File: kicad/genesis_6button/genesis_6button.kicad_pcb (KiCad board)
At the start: 2 copper layers, 61.7 x 36.8 mm, 27 parts, among them J1 Conn_02x07_Odd_Even, J2 DB9_Female, J3 Conn_02x03_Odd_Even, U1 74HC257, U2 ATtiny404-SS, U3 74HC257

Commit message: Revert to first revision of PCB
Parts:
- removed C4: 10u, Capacitor_THT:CP_Radial_D8.0mm_P5.00mm
- removed H1: MountingHole, MountingHole:MountingHole_5.3mm_M5
- removed R13, R14: 100k, Resistor_SMD:R_0805_2012Metric
- removed TP1, TP2: TestPoint, TestPoint:TestPoint_Loop_D3.50mm_Drill0.9mm_Beaded
- C1, C2, C3: footprint Capacitor_SMD:C_1206_3216Metric -> Capacitor_SMD:C_0805_2012Metric
- R1, R10, R11, R12, R2, R3, R4, R5, R6, R7, R8, R9: value 75k -> 47k
- moved R4 16.5 mm to (108.0, 52.8), turned to 180 degrees
- moved R5 15.8 mm to (108.0, 50.3), turned to 180 degrees
- moved R11 14.4 mm to (108.0, 60.5), turned to 180 degrees
- moved R6 12.2 mm to (108.0, 47.8), turned to 180 degrees
- moved R12 11.4 mm to (108.0, 57.9), turned to 180 degrees
- moved R10 9.76 mm to (112.4, 60.5), turned to 0 degrees
- moved R7 9.15 mm to (108.0, 63.0), turned to 180 degrees
- moved R1 8.10 mm to (112.4, 52.8), turned to 0 degrees
- moved J1 8.05 mm to (97.2, 47.8)
- moved R3 7.22 mm to (112.4, 47.8), turned to 0 degrees
- moved R8 6.67 mm to (112.4, 63.0), turned to 0 degrees
- moved R9 6.43 mm to (112.4, 57.9), turned to 0 degrees
- moved J2 4.96 mm to (154.9, 45.8)
- moved R2 4.65 mm to (112.4, 50.3), turned to 0 degrees
- moved C1 4.31 mm to (131.7, 44.8), turned to 270 degrees
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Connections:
- U2 pad 3: BUTTON_MODE -> (no net)
- U3 pad 2: BUTTON_DOWN -> BUTTON_UP
- U3 pad 3: BUTTON_Y -> BUTTON_Z
- U3 pad 4: DOWN -> UP
- U3 pad 5: BUTTON_UP -> BUTTON_DOWN
- U3 pad 6: BUTTON_Z -> BUTTON_Y
- U3 pad 7: UP -> DOWN
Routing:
- net Net-(J3-Pad1): track 30.3 -> 77.9 mm, vias 1 -> 2
- net BUTTON_Z: track 35.9 -> 74.1 mm
- net BUTTON_Y: track 29.6 -> 64.9 mm, vias 1 -> 2
- net BUTTON_X: track 39.0 -> 71.4 mm, vias 3 -> 2
- net DOWN: track 52.2 -> 81.8 mm, vias 4 -> 1
- net +5V: track 138.6 -> 168.2 mm, vias 6 -> 5
- net BUTTON_LEFT: track 48.5 -> 69.0 mm, vias 2 -> 3
- net Net-(U2-Pad5): track 41.7 -> 28.9 mm
- net UP: track 66.3 -> 76.4 mm, vias 2 -> 1
- net BUTTON_C: track 21.0 -> 30.4 mm, vias 0 -> 1
- net BUTTON_DOWN: track 25.0 -> 34.1 mm
- net BUTTON_B: track 22.6 -> 31.2 mm, vias 0 -> 1
- net BUTTON_A: track 25.9 -> 34.0 mm, vias 2 -> 3
- net BUTTON_UP: track 22.7 -> 29.0 mm
- net RIGHT: track 52.7 -> 46.6 mm, vias 3 -> 2
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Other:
- board size 61.7 x 36.8 mm -> 73.7 x 36.8 mm
- board text removed: "+5V"
- board text removed: "GND"

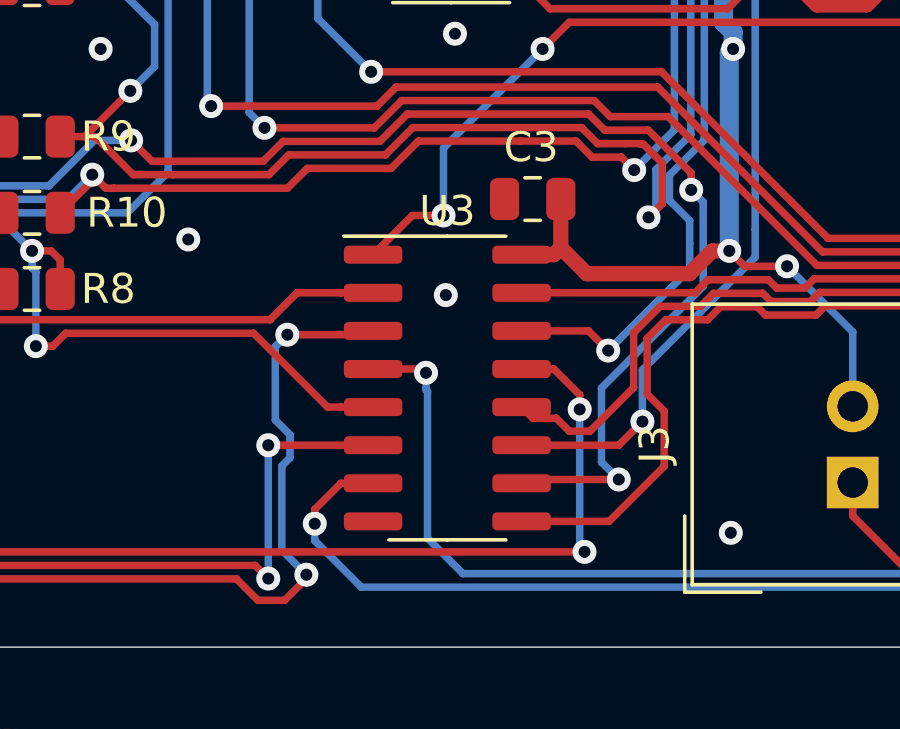
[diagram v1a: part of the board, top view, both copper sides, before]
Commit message: Move U3 slightly to fix a thermal relief error
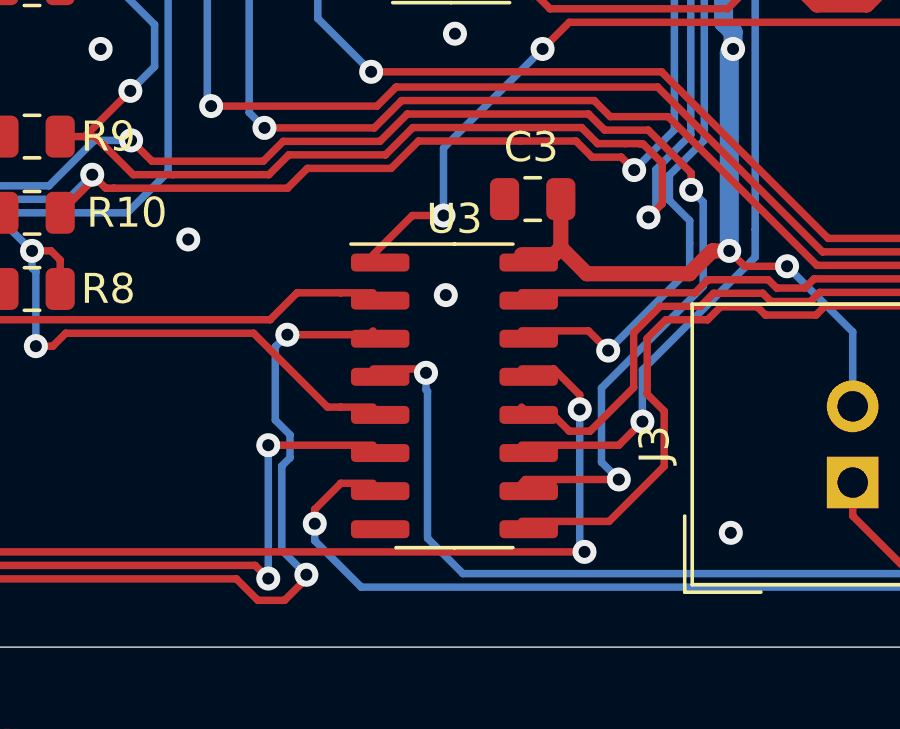
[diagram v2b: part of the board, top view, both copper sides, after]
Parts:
- moved U3 0.35 mm to (126.5, 66.6)
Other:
- net class Default removed

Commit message: Add extra labels to front silkscreen
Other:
- board text added: "1"
- board text added: "6 button Sega Mega Drive controller PCB"
- board text added: "ATtiny404"
- board text added: "USBtinyISP"
- board text added: "https://github.com/rfmerrill/genesis_6button 2022"
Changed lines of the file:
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@@
 		(0 "F.Cu" signal)
 		(2 "B.Cu" signal)
-		(9 "F.Adhes" user)
-		(11 "B.Adhes" user)
+		(9 "F.Adhes" user "F.Adhesive")
+		(11 "B.Adhes" user "B.Adhesive")
 		(13 "F.Paste" user)
 		(15 "B.Paste" user)
-		(5 "F.SilkS" user)
-		(7 "B.SilkS" user)
+		(5 "F.SilkS" user "F.Silkscreen")
+		(7 "B.SilkS" user "B.Silkscreen")
 		(1 "F.Mask" user)
 		(3 "B.Mask" user)
-		(17 "Dwgs.User" user)
-		(19 "Cmts.User" user)
-		(21 "Eco1.User" user)
-		(23 "Eco2.User" user)
+		(17 "Dwgs.User" user "User.Drawings")
+		(19 "Cmts.User" user "User.Comments")
+		(21 "Eco1.User" user "User.Eco1")
+		(23 "Eco2.User" user "User.Eco2")
 		(25 "Edge.Cuts" user)
 		(27 "Margin" user)
-		(31 "F.CrtYd" user)
-		(29 "B.CrtYd" user)
+		(31 "F.CrtYd" user "F.Courtyard")
+		(29 "B.CrtYd" user "B.Courtyard")
 		(35 "F.Fab" user)
 		(33 "B.Fab" user)
@@
 		(layer "Edge.Cuts")
 	)
+	(gr_text "USBtinyISP"
+		(at 138.049 62.4078 0)
+		(layer "F.SilkS")
+		(effects
+			(font
+				(size 1 1)
+				(thickness 0.15)
+			)
+			(justify left bottom)
+		)
+	)
+	(gr_text "1"
+		(at 156.27 47.117 0)
+		(layer "F.SilkS")
+		(effects
+			(font
+				(size 1 1)
+				(thickness 0.15)
+			)
+			(justify left bottom)
+		)
+	)
+	(gr_text "https://github.com/rfmerrill/genesis_6button 2022"
+		(at 89.3572 74.4982 0)
+		(layer "F.SilkS")
+		(effects
+			(font
+				(size 1 1)
+				(thickness 0.15)
+			)
+			(justify left bottom)
+		)
+	)
+	(gr_text "ATtiny404"
+		(at 140.98 49.657 0)
+		(layer "F.SilkS")
+		(effects
+			(font
+				(size 1 1)
+				(thickness 0.15)
+			)
+			(justify left bottom)
+		)
+	)
+	(gr_text "6 button Sega Mega Drive controller PCB"
+		(at 89.8398 40.1828 0)
+		(layer "F.SilkS")
+		(effects
+			(font
+				(size 1 1)
+				(thickness 0.25)
+				(bold yes)
+			)
+			(justify left bottom)
+		)
+	)
 	(segment

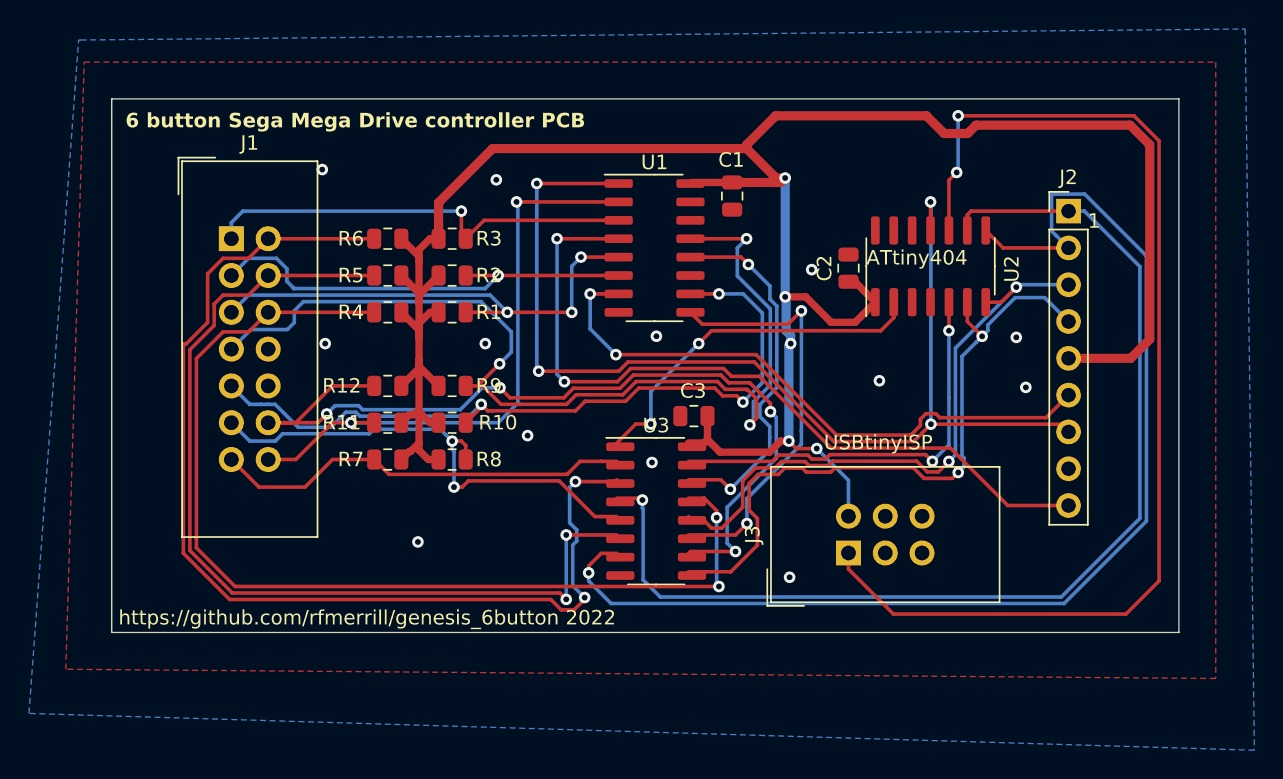
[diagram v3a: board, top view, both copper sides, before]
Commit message: Add version number to front silkscreen
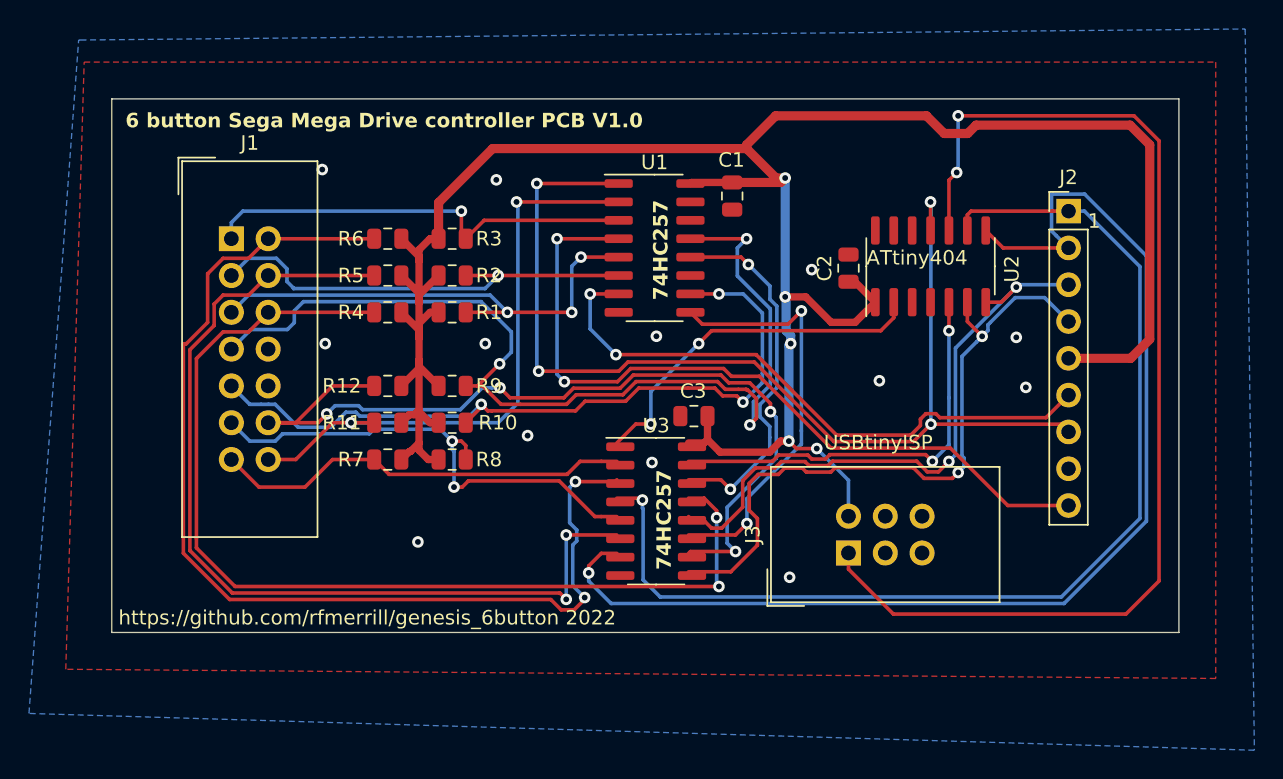
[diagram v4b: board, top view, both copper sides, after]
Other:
- board text added: "6 button Sega Mega Drive controller PCB V1.0"
- board text added: "74HC257"
- board text removed: "6 button Sega Mega Drive controller PCB"
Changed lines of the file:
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@@
+		)
+	)
+	(gr_text "74HC257"
+		(at 127.381 51.9938 90)
+		(layer "F.SilkS")
+		(effects
+			(font
+				(size 1 1)
+				(thickness 0.25)
+				(bold yes)
+			)
+			(justify left bottom)
 		)
 	)
@@
 		)
 	)
-	(gr_text "6 button Sega Mega Drive controller PCB"
+	(gr_text "74HC257"
+		(at 127.6096 70.612 90)
+		(layer "F.SilkS")
+		(effects
+			(font
+				(size 1 1)
+				(thickness 0.25)
+				(bold yes)
+			)
+			(justify left bottom)
+		)
+	)
+	(gr_text "6 button Sega Mega Drive controller PCB V1.0"
 		(at 89.8398 40.1828 0)
 		(layer "F.SilkS")

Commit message: Add M2 mount holes
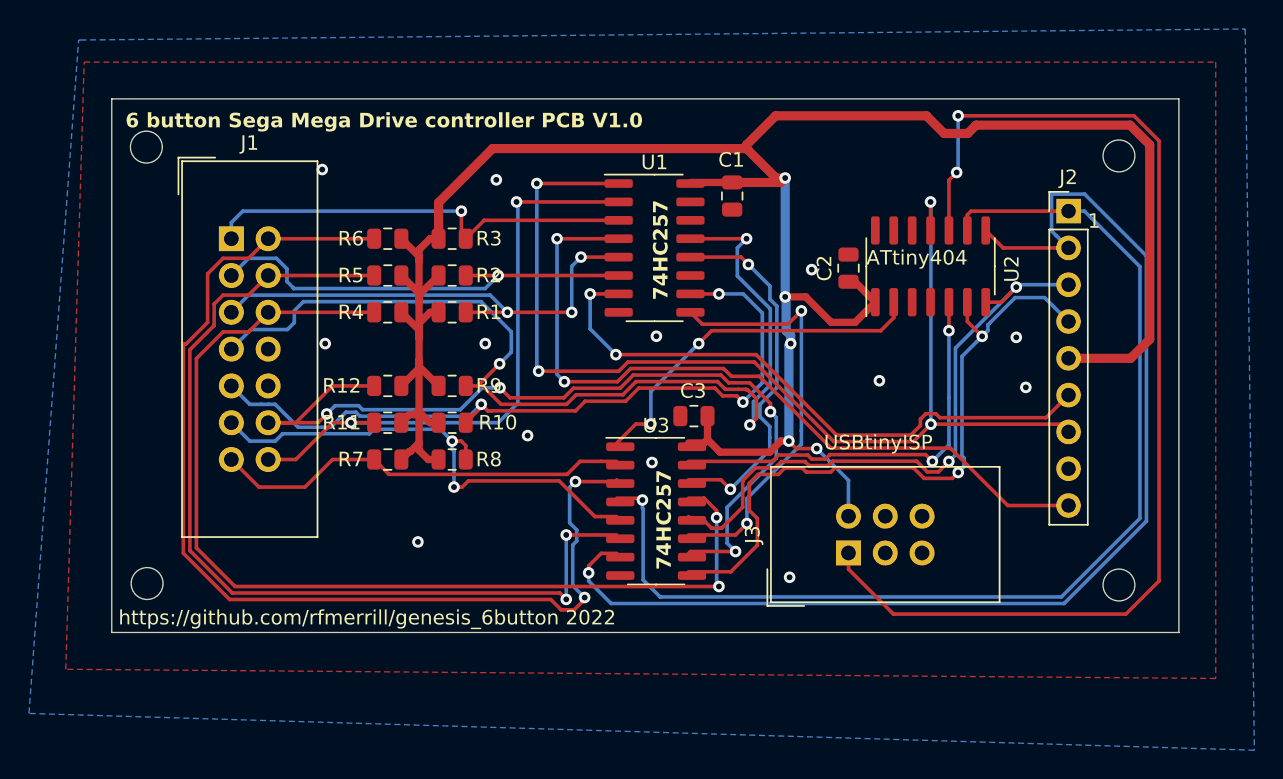
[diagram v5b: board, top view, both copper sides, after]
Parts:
- added H1: MountingHole, MountingHole:MountingHole_2.2mm_M2, F.Cu at (91.3, 41.4)
- added H2: MountingHole, MountingHole:MountingHole_2.2mm_M2, F.Cu at (158.4, 42.0)
- added H3: MountingHole, MountingHole:MountingHole_2.2mm_M2, F.Cu at (91.3, 71.6)
- added H4: MountingHole, MountingHole:MountingHole_2.2mm_M2, F.Cu at (158.4, 71.7)
- R1, R10, R11, R12, R2, R3, R4, R5, R6, R7, R8, R9: value 47k -> 75k
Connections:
- J3 pad 3: (no net) -> unconnected-(J3-Pin_3-Pad3)
- J3 pad 4: (no net) -> unconnected-(J3-Pin_4-Pad4)
- J3 pad 5: (no net) -> unconnected-(J3-Pin_5-Pad5)
- U2 pad 12: (no net) -> unconnected-(U2-PA2-Pad12)
- U2 pad 13: (no net) -> unconnected-(U2-PA3-Pad13)
- U2 pad 3: (no net) -> unconnected-(U2-PA5-Pad3)
- U2 pad 4: (no net) -> unconnected-(U2-PA6-Pad4)

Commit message: Add buttons to silkscreen
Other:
- board text added: "A"
- board text added: "B"
- board text added: "C"
- board text added: "D"
- board text added: "G"
- board text added: "L"
- board text added: "M"
- board text added: "R"
- board text added: "S"
- board text added: "U"
- board text added: "X"
- board text added: "Y"
- board text added: "Z"
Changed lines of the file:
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@@
 		(layer "Edge.Cuts")
+	)
+	(gr_text "D"
+		(at 94 61.5 0)
+		(layer "F.SilkS")
+		(effects
+			(font
+				(size 1.5 1.5)
+				(thickness 0.3)
+				(bold yes)
+			)
+			(justify left bottom)
+		)
+	)
+	(gr_text "R"
+		(at 94 59 0)
+		(layer "F.SilkS")
+		(effects
+			(font
+				(size 1.5 1.5)
+				(thickness 0.3)
+				(bold yes)
+			)
+			(justify left bottom)
+		)
+	)
+	(gr_text "Z"
+		(at 101 48 0)
+		(layer "F.SilkS")
+		(effects
+			(font
+				(size 1.5 1.5)
+				(thickness 0.3)
+				(bold yes)
+			)
+			(justify left bottom)
+		)
+	)
+	(gr_text "G"
+		(at 101 56.5 0)
+		(layer "F.SilkS")
+		(effects
+			(font
+				(size 1.5 1.5)
+				(thickness 0.3)
+				(bold yes)
+			)
+			(justify left bottom)
+		)
 	)
 	(gr_text "USBtinyISP"
@@
 		)
 	)
+	(gr_text "L"
+		(at 94 56.5 0)
+		(layer "F.SilkS")
+		(effects
+			(font
+				(size 1.5 1.5)
+				(thickness 0.3)
+				(bold yes)
+			)
+			(justify left bottom)
+		)
+	)
+	(gr_text "Y"
+		(at 101 51 0)
+		(layer "F.SilkS")
+		(effects
+			(font
+				(size 1.5 1.5)
+				(thickness 0.3)
+				(bold yes)
+			)
+			(justify left bottom)
+		)
+	)
+	(gr_text "S"
+		(at 101 64 0)
+		(layer "F.SilkS")
+		(effects
+			(font
+				(size 1.5 1.5)
+				(thickness 0.3)
+				(bold yes)
+			)
+			(justify left bottom)
+		)
+	)
 	(gr_text "1"
 		(at 156.27 47.117 0)
@@
 		)
 	)
+	(gr_text "C"
+		(at 94 48 0)
+		(layer "F.SilkS")
+		(effects
+			(font
+				(size 1.5 1.5)
+				(thickness 0.3)
+				(bold yes)
+			)
+			(justify left bottom)
+		)
+	)
+	(gr_text "M"
+		(at 101 61.5 0)
+		(layer "F.SilkS")
+		(effects
+			(font
+				(size 1.5 1.5)
+				(thickness 0.3)
+				(bold yes)
+			)
+			(justify left bottom)
+		)
+	)
+	(gr_text "G"
+		(at 101 59 0)
+		(layer "F.SilkS")
+		(effects
+			(font
+				(size 1.5 1.5)
+				(thickness 0.3)
+				(bold yes)
+			)
+			(justify left bottom)
+		)
+	)
+	(gr_text "A"
+		(at 94 54 0)
+		(layer "F.SilkS")
+		(effects
+			(font
+				(size 1.5 1.5)
+				(thickness 0.3)
+				(bold yes)
+			)
+			(justify left bottom)
+		)
+	)
 	(gr_text "https://github.com/rfmerrill/genesis_6button 2022"
 		(at 89.3572 74.4982 0)
@@
 		)
 	)
+	(gr_text "U"
+		(at 94 64 0)
+		(layer "F.SilkS")
+		(effects
+			(font
+				(size 1.5 1.5)
+				(thickness 0.3)
+				(bold yes)
+			)
+			(justify left bottom)
+		)
+	)
 	(gr_text "74HC257"
 		(at 127.381 51.9938 90)
@@
 				(bold yes)
 			)
+			(justify left bottom)
+		)
+	)
+	(gr_text "X"
+		(at 101 54 0)
+		(layer "F.SilkS")
+		(effects
+			(font
+				(size 1.5 1.5)
+				(thickness 0.3)
+				(bold yes)
+			)
+			(justify left bottom)
+		)
+	)
+	(gr_text "B"
+		(at 94 51 0)
+		(layer "F.SilkS")
+		(effects
+			(font
+				(size 1.5 1.5)
+				(thickness 0.3)
+				(bold yes)
+			)
